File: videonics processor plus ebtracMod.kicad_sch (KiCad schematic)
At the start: 0 parts

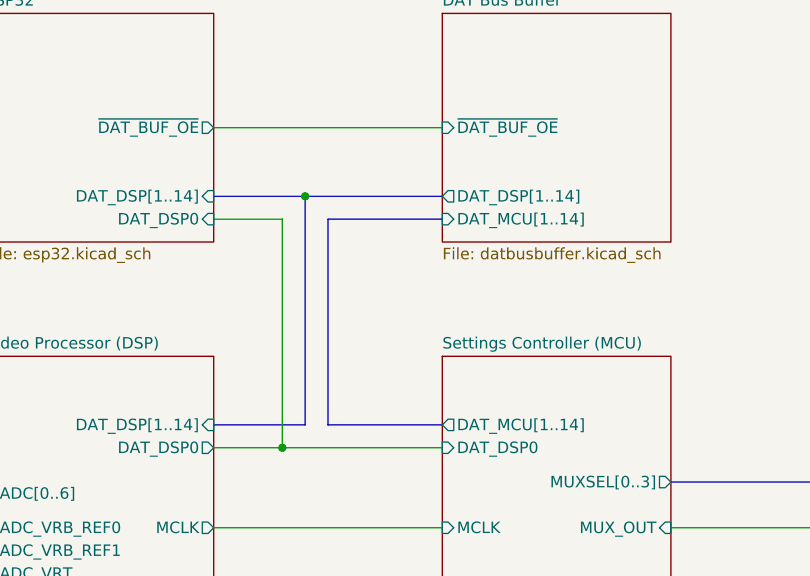
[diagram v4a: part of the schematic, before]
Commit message: added vid_blk and fixed inverter on dat 0
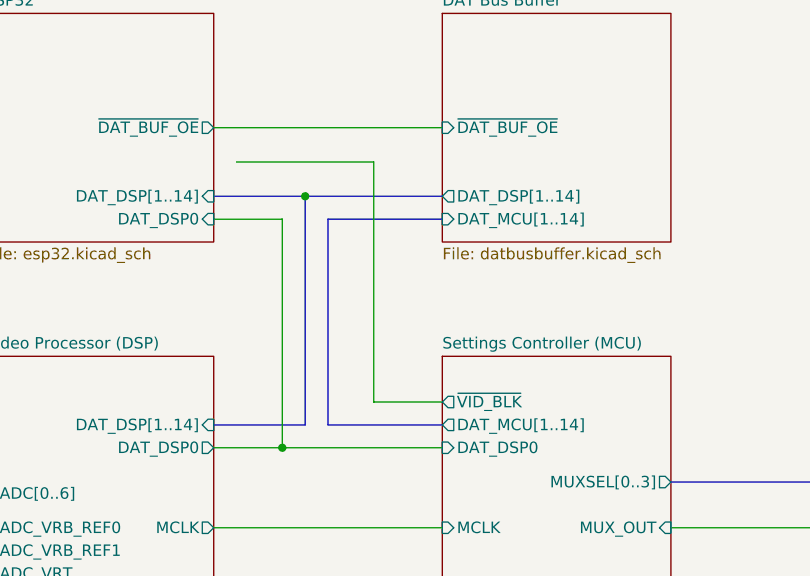
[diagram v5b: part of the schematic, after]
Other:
- sheet Settings Controller (MCU) ports: added ~{VID_BLK}; removed none
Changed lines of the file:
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@@
+    (stroke (width 0) (type default) (color 0 0 0 0))
+  )
+  (wire (pts (xy 119.38 68.58) (xy 119.38 41.91))
     (stroke (width 0) (type default) (color 0 0 0 0))
   )
@@
     (stroke (width 0) (type default) (color 0 0 0 0))
   )
+  (wire (pts (xy 127 68.58) (xy 119.38 68.58))
+    (stroke (width 0) (type default) (color 0 0 0 0))
+  )
   (wire (pts (xy 109.22 48.26) (xy 109.22 73.66))
     (stroke (width 0) (type default) (color 0 0 0 0))
@@
   )
   (bus (pts (xy 203.2 148.59) (xy 217.17 148.59))
+    (stroke (width 0) (type default) (color 0 0 0 0))
+  )
+  (wire (pts (xy 104.14 41.91) (xy 119.38 41.91))
     (stroke (width 0) (type default) (color 0 0 0 0))
   )
@@
     )
     (pin "DAT_MCU[1..14]" output (at 127 71.12 180)
+      (effects (font (size 1.27 1.27)) (justify left))
+    )
+    (pin "~{VID_BLK}" output (at 127 68.58 180)
       (effects (font (size 1.27 1.27)) (justify left))
     )
@@
       (reference "#PWR0250") (unit 1) (value "+5V") (footprint "")
     )
+    (path "/b0d0a36a-2958-4482-a6bb-9b3de3eee92b/f217cbb2-2b10-4603-95e2-89b2a6bd290f"
+      (reference "#PWR0251") (unit 1) (value "GND") (footprint "")
+    )
+    (path "/b0d0a36a-2958-4482-a6bb-9b3de3eee92b/8bf46615-f175-4d6d-82be-5b65147a6e8e"
+      (reference "#PWR0252") (unit 1) (value "+3.3V") (footprint "")
+    )
     (path "/b0d0a36a-2958-4482-a6bb-9b3de3eee92b/bd4044f5-8100-4003-88c6-95fffda0312a"
       (reference "#PWR0258") (unit 1) (value "GND") (footprint "")
@@
       (reference "J15") (unit 1) (value "DAT_DSP_9..14") (footprint "Connector_PinHeader_2.54mm:PinHeader_1x06_P2.54mm_Vertical")
     )
+    (path "/b0d0a36a-2958-4482-a6bb-9b3de3eee92b/7bc98a8b-777e-4ee8-9be7-8bb737e75131"
+      (reference "J16") (unit 1) (value "~{VID_BLK}") (footprint "Connector_PinHeader_2.54mm:PinHeader_1x01_P2.54mm_Vertical")
+    )
     (path "/b9e696c4-ae03-4bea-bb3e-e63111859237/baeca21f-e3e8-461d-832f-da5986f424d1"
       (reference "JP1") (unit 1) (value "Conn_02x13_Odd_Even") (footprint "")
@@
       (reference "Q16") (unit 1) (value "2N3904") (footprint "Package_TO_SOT_THT:TO-92_Inline")
     )
+    (path "/b0d0a36a-2958-4482-a6bb-9b3de3eee92b/64cebd65-c0dd-4ded-b22f-83a287d6d639"
+      (reference "Q17") (unit 1) (value "2N3904") (footprint "Package_TO_SOT_THT:TO-92_Inline_Wide")
+    )
     (path "/b0d0a36a-2958-4482-a6bb-9b3de3eee92b/88656a7b-8df1-4faf-ac86-c791d10d969c"
       (reference "Q20") (unit 1) (value "2N3904") (footprint "Package_TO_SOT_THT:TO-92_Inline_Wide")
@@
       (reference "R92") (unit 1) (value "10k") (footprint "Resistor_THT:R_Axial_DIN0207_L6.3mm_D2.5mm_P2.54mm_Vertical")
     )
+    (path "/b0d0a36a-2958-4482-a6bb-9b3de3eee92b/44fff87e-8dd5-4438-bd40-297147bd030e"
+      (reference "R93") (unit 1) (value "10k") (footprint "Resistor_THT:R_Axial_DIN0207_L6.3mm_D2.5mm_P2.54mm_Vertical")
+    )
+    (path "/b0d0a36a-2958-4482-a6bb-9b3de3eee92b/71407b5b-5c0a-4b7b-99ff-b2a846f52acc"
+      (reference "R94") (unit 1) (value "220k") (footprint "Resistor_THT:R_Axial_DIN0207_L6.3mm_D2.5mm_P2.54mm_Vertical")
+    )
     (path "/b0d0a36a-2958-4482-a6bb-9b3de3eee92b/c9f7de88-f8bf-4f1a-84cd-843eb46645d8"

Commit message: import heirarchical pin
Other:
- sheet ESP32 ports: added ~{VID_BLK}; removed none
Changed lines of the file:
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@@
     (stroke (width 0) (type default) (color 0 0 0 0))
   )
-  (wire (pts (xy 104.14 41.91) (xy 119.38 41.91))
+  (wire (pts (xy 101.6 41.91) (xy 119.38 41.91))
     (stroke (width 0) (type default) (color 0 0 0 0))
   )
@@
       (effects (font (size 1.27 1.27)) (justify right))
     )
+    (pin "~{VID_BLK}" input (at 101.6 41.91 0)
+      (effects (font (size 1.27 1.27)) (justify right))
+    )
